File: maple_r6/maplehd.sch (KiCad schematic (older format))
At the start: 0 parts

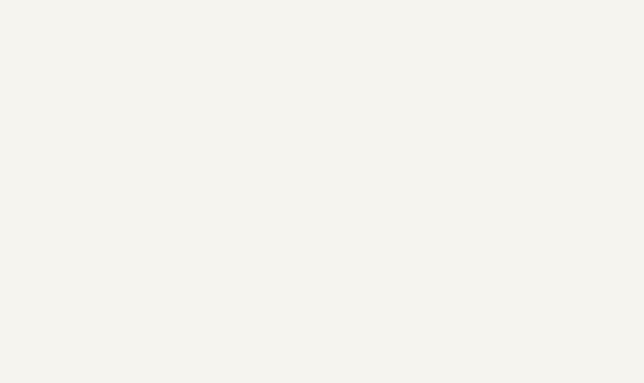
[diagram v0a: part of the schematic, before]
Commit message: R6v1 : Updated schematic and created PCB layout
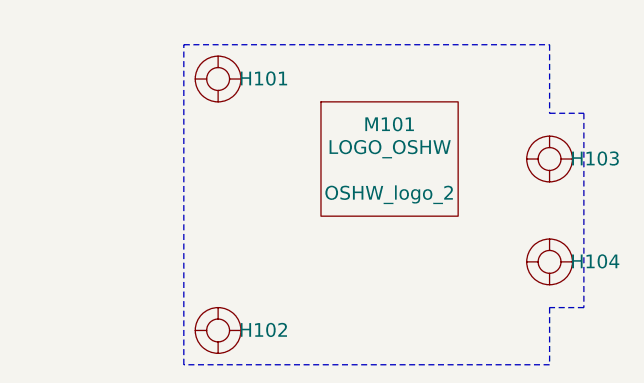
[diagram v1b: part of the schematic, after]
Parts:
- added H101, H102, H103, H104: HOLE_RMC, ~, symbol HOLE_RMC
- added M101: LOGO_OSHW, OSHW_logo_2, symbol LOGO_OSHW
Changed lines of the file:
@@
-EESchema Schematic File Version 2  date Tue 07 Jun 2011 10:30:22 AM PDT
-LIBS:power,/home/jessb/Projects/leafhw/hardware-lib/leaf,/home/jessb/Documents/st-microelectronics,device,transistors,conn,linear,regul,74xx,cmos4000,adc-dac,memory,xilinx,special,microcontrollers,dsp,microchip,analog_switches,motorola,texas,intel,audio,interface,digital-audio,philips,display,cypress,siliconi,opto,atmel,contrib,valves
-EELAYER 43  0
+EESchema Schematic File Version 2
+LIBS:leaf
+LIBS:power
+LIBS:st-microelectronics
+LIBS:device
+LIBS:transistors
+LIBS:conn
+LIBS:linear
+LIBS:regul
+LIBS:74xx
+LIBS:cmos4000
+LIBS:adc-dac
+LIBS:memory
+LIBS:xilinx
+LIBS:special
+LIBS:microcontrollers
+LIBS:dsp
+LIBS:microchip
+LIBS:analog_switches
+LIBS:motorola
+LIBS:texas
+LIBS:intel
+LIBS:audio
+LIBS:interface
+LIBS:digital-audio
+LIBS:philips
+LIBS:display
+LIBS:cypress
+LIBS:siliconi
+LIBS:opto
+LIBS:atmel
+LIBS:contrib
+LIBS:valves
+LIBS:RMC
+LIBS:maplehd-cache
+EELAYER 27 0
 EELAYER END
-$Descr A4 11700 8267
+$Descr A4 11693 8268
+encoding utf-8
 Sheet 1 3
 Title ""
-Date "6 jun 2011"
+Date "11 may 2015"
 Rev ""
 Comp ""
@@
 F1 "pwr.sch" 60
 $EndSheet
+$Comp
+L HOLE_RMC H102
+U 1 1 554F6219
+P 9000 4400
+F 0 "H102" H 9200 4400 60  0000 C CNN
+F 1 "HOLE_RMC" H 9000 4550 60  0001 C CNN
+F 2 "~" H 9000 4400 60  0000 C CNN
+F 3 "~" H 9000 4400 60  0000 C CNN
+	1    9000 4400
+	1    0    0    -1
+$EndComp
+$Comp
+L HOLE_RMC H101
+U 1 1 554F621F
+P 9000 3300
+F 0 "H101" H 9200 3300 60  0000 C CNN
+F 1 "HOLE_RMC" H 9000 3450 60  0001 C CNN
+F 2 "~" H 9000 3300 60  0000 C CNN
+F 3 "~" H 9000 3300 60  0000 C CNN
+	1    9000 3300
+	1    0    0    -1
+$EndComp
+$Comp
+L HOLE_RMC H104
+U 1 1 554F6243
+P 10450 4100
+F 0 "H104" H 10650 4100 60  0000 C CNN
+F 1 "HOLE_RMC" H 10450 4250 60  0001 C CNN
+F 2 "~" H 10450 4100 60  0000 C CNN
+F 3 "~" H 10450 4100 60  0000 C CNN
+	1    10450 4100
+	1    0    0    -1
+$EndComp
+$Comp
+L HOLE_RMC H103
+U 1 1 554F6249
+P 10450 3650
+F 0 "H103" H 10650 3650 60  0000 C CNN
+F 1 "HOLE_RMC" H 10450 3800 60  0001 C CNN
+F 2 "~" H 10450 3650 60  0000 C CNN
+F 3 "~" H 10450 3650 60  0000 C CNN
+	1    10450 3650
+	1    0    0    -1
+$EndComp
+$Comp
+L LOGO_OSHW M101
+U 1 1 554F631F
+P 9750 3650
+F 0 "M101" H 9750 3800 60  0000 C CNN
+F 1 "LOGO_OSHW" H 9750 3700 60  0000 C CNN
+F 2 "OSHW_logo_2" H 9750 3500 60  0000 C CNN
+F 3 "~" H 9750 3650 60  0000 C CNN
+	1    9750 3650
+	1    0    0    -1
+$EndComp
+Wire Notes Line
+	8850 3150 10450 3150
+Wire Notes Line
+	10450 3150 10450 3450
+Wire Notes Line
+	10450 3450 10600 3450
+Wire Notes Line
+	10600 3450 10600 4300
+Wire Notes Line
+	10600 4300 10450 4300
+Wire Notes Line
+	10450 4300 10450 4550
+Wire Notes Line
+	10450 4550 8850 4550
+Wire Notes Line
+	8850 4550 8850 3150
 $EndSCHEMATC
